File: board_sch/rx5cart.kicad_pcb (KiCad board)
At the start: 2 copper layers, 140.7 x 101.8 mm, 9 parts, among them P1 RX5_WDC, U1 TEENSYPP2, U2 TC551001, U3 TC551001

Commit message: Add RX5 power sense
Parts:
- moved D1 18.8 mm to (72.4, 116.0)
- moved P1 18.8 mm to (29.5, 110.0)
- moved U2 18.8 mm to (116.3, 54.6)
- moved R1 18.8 mm to (156.2, 119.4)
- moved U1 18.8 mm to (91.0, 73.7)
- moved C2 18.8 mm to (158.8, 104.1)
- moved D2 18.8 mm to (143.5, 118.1)
- moved U3 18.8 mm to (147.3, 54.6)
- moved C1 18.8 mm to (158.8, 110.5)
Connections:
- U1 pad 43: (no net) -> Net-(D1-Pad1)
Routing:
- net Net-(D1-Pad1): track 34.2 -> 96.2 mm
- net VCC: track 261.8 -> 256.8 mm
- net /OE: track 268.4 -> 267.7 mm
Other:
- board text added: "Max Pastushkov's RX5Cart Based on GliGli's RX5USB"
- board text added: "Rev 1.0"
- board text removed: "Max Pastushkov's RX5Cart Based on GliGli's RX5USB rev 2.8"

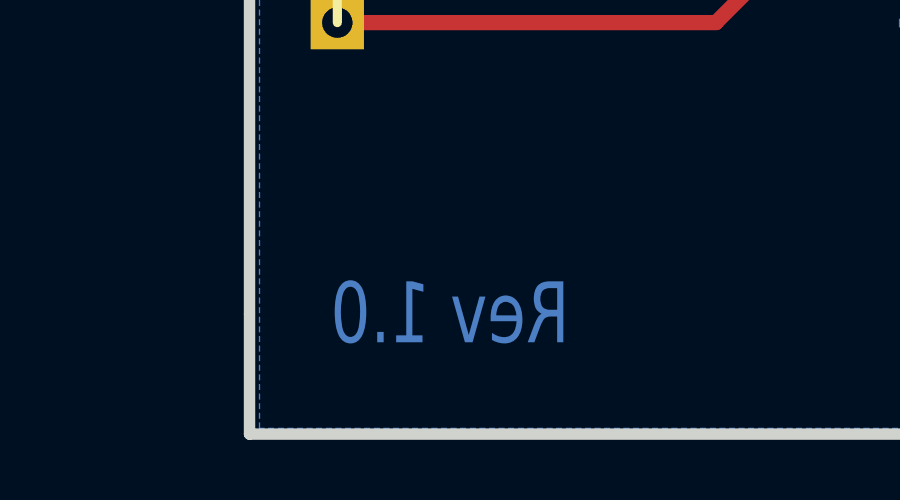
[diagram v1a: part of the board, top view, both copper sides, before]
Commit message: Change revision number
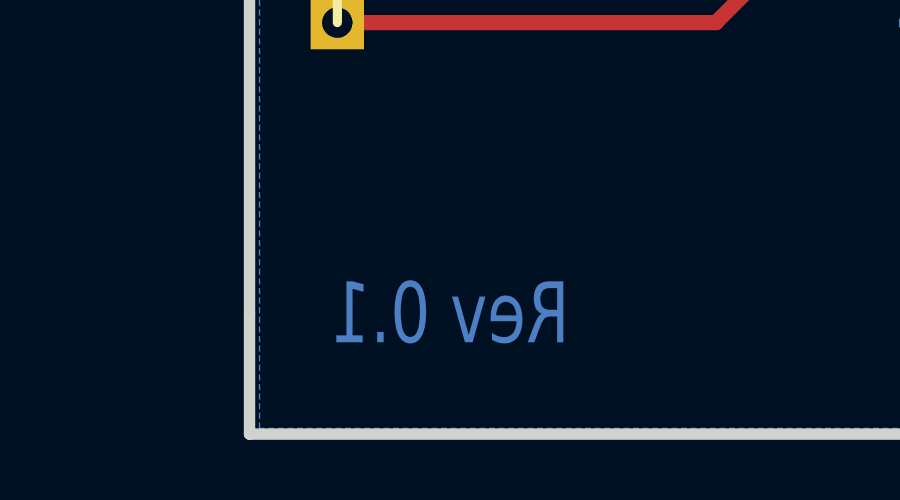
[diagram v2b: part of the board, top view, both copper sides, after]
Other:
- board text added: "Rev 0.1"
- board text removed: "Rev 1.0"
